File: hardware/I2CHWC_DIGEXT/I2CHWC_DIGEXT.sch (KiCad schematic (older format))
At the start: 63 parts, among them J1 Encoders 11-20, J2 Encoders 21-30, J3 EXT

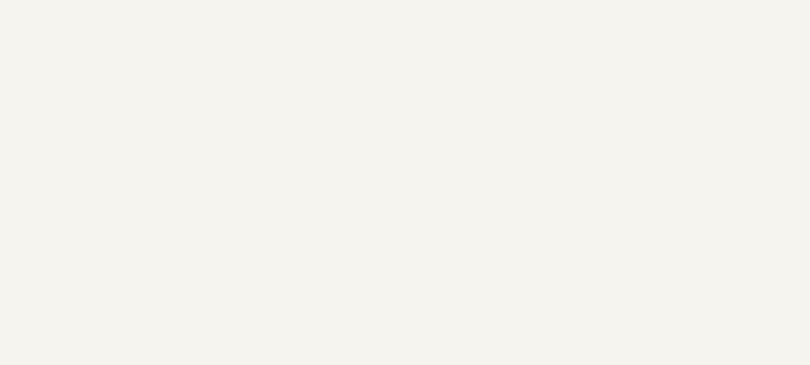
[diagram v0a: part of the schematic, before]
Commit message: Firmwware changes: Temporarily disable ADC (whilst investigating noise issues). Change quantity of switches (from 60 to 50). Start implementing I2C commands (wip). Reverse encoder rotation (maybe just the hardware implementation of the prototype - need to validate with schematics). Schematic and PCB improvements (wip): Separate out main and extender boards to separate projects / folders. Main board now supports 10 encoders with switches, 20 switches and 8 ADC plus detection of ADC multiplex and I2C address. Extension board for encoders 11 - 30. Extension board for ADC 1 - 64.
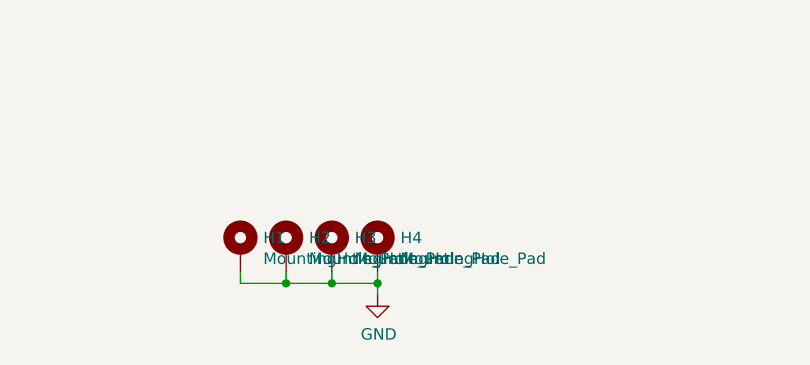
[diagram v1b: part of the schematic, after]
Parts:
- added H1, H2, H3, H4: MountingHole_Pad, MountingHole:MountingHole_3.2mm_M3_Pad_Via, symbol Mechanical:MountingHole_Pad
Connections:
- new net GND: H1.1, H2.1, H3.1, H4.1
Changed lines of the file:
@@
 EESchema Schematic File Version 4
+LIBS:I2CHWC_DIGEXT-cache
 EELAYER 29 0
 EELAYER END
@@
 encoding utf-8
 Sheet 1 1
-Title ""
-Date ""
-Rev ""
-Comp ""
-Comment1 ""
+Title "I2C HWC Digital Extender"
+Date "2019-03-28"
+Rev "1"
+Comp "riban"
+Comment1 "https://github.com/riban-bw/I2C-Hardware-Controller"
 Comment2 ""
-Comment3 ""
-Comment4 ""
+Comment3 "Provides rotary encoders 11 - 30"
+Comment4 "Extender board for riban I2C HWC"
 $EndDescr
 $Comp
@@
 NoConn ~ 7700 1950
 NoConn ~ 7700 1850
+$Comp
+L Mechanical:MountingHole_Pad H1
+U 1 1 5CA14710
+P 5650 6900
+F 0 "H1" H 5750 6949 50  0000 L CNN
+F 1 "MountingHole_Pad" H 5750 6858 50  0000 L CNN
+F 2 "MountingHole:MountingHole_3.2mm_M3_Pad_Via" H 5650 6900 50  0001 C CNN
+F 3 "~" H 5650 6900 50  0001 C CNN
+	1    5650 6900
+	1    0    0    -1
+$EndComp
+$Comp
+L Mechanical:MountingHole_Pad H2
+U 1 1 5CA14A13
+P 5850 6900
+F 0 "H2" H 5950 6949 50  0000 L CNN
+F 1 "MountingHole_Pad" H 5950 6858 50  0000 L CNN
+F 2 "MountingHole:MountingHole_3.2mm_M3_Pad_Via" H 5850 6900 50  0001 C CNN
+F 3 "~" H 5850 6900 50  0001 C CNN
+	1    5850 6900
+	1    0    0    -1
+$EndComp
+$Comp
+L Mechanical:MountingHole_Pad H3
+U 1 1 5CA14A61
+P 6050 6900
+F 0 "H3" H 6150 6949 50  0000 L CNN
+F 1 "MountingHole_Pad" H 6150 6858 50  0000 L CNN
+F 2 "MountingHole:MountingHole_3.2mm_M3_Pad_Via" H 6050 6900 50  0001 C CNN
+F 3 "~" H 6050 6900 50  0001 C CNN
+	1    6050 6900
+	1    0    0    -1
+$EndComp
+$Comp
+L Mechanical:MountingHole_Pad H4
+U 1 1 5CA14A92
+P 6250 6900
+F 0 "H4" H 6350 6949 50  0000 L CNN
+F 1 "MountingHole_Pad" H 6350 6858 50  0000 L CNN
+F 2 "MountingHole:MountingHole_3.2mm_M3_Pad_Via" H 6250 6900 50  0001 C CNN
+F 3 "~" H 6250 6900 50  0001 C CNN
+	1    6250 6900
+	1    0    0    -1
+$EndComp
+$Comp
+L power:GND #PWR?
+U 1 1 5CA2BF9E
+P 6250 7100
+F 0 "#PWR?" H 6250 6850 50  0001 C CNN
+F 1 "GND" H 6255 6927 50  0000 C CNN
+F 2 "" H 6250 7100 50  0001 C CNN
+F 3 "" H 6250 7100 50  0001 C CNN
+	1    6250 7100
+	1    0    0    -1
+$EndComp
+Wire Wire Line
+	5650 7000 5650 7050
+Wire Wire Line
+	5650 7050 5850 7050
+Wire Wire Line
+	6250 7050 6250 7000
+Wire Wire Line
+	6250 7100 6250 7050
+Connection ~ 6250 7050
+Wire Wire Line
+	6050 7050 6050 7000
+Connection ~ 6050 7050
+Wire Wire Line
+	6050 7050 6250 7050
+Wire Wire Line
+	5850 7050 5850 7000
+Connection ~ 5850 7050
+Wire Wire Line
+	5850 7050 6050 7050
 $EndSCHEMATC
